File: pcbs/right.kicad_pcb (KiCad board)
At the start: 2 copper layers, 132.7 x 86.8 mm, 46 parts

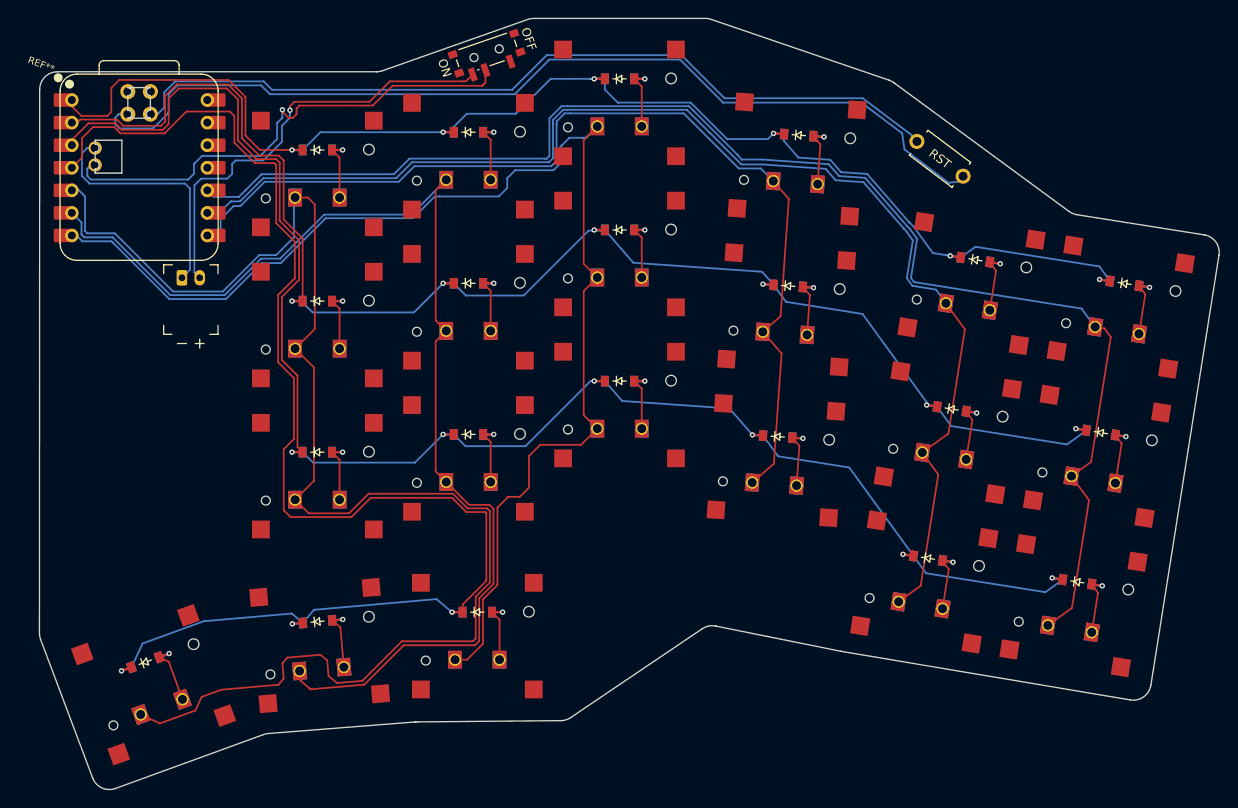
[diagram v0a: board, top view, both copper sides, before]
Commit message: improved some of the routing. added cutout for batter to save 1mm during assembly
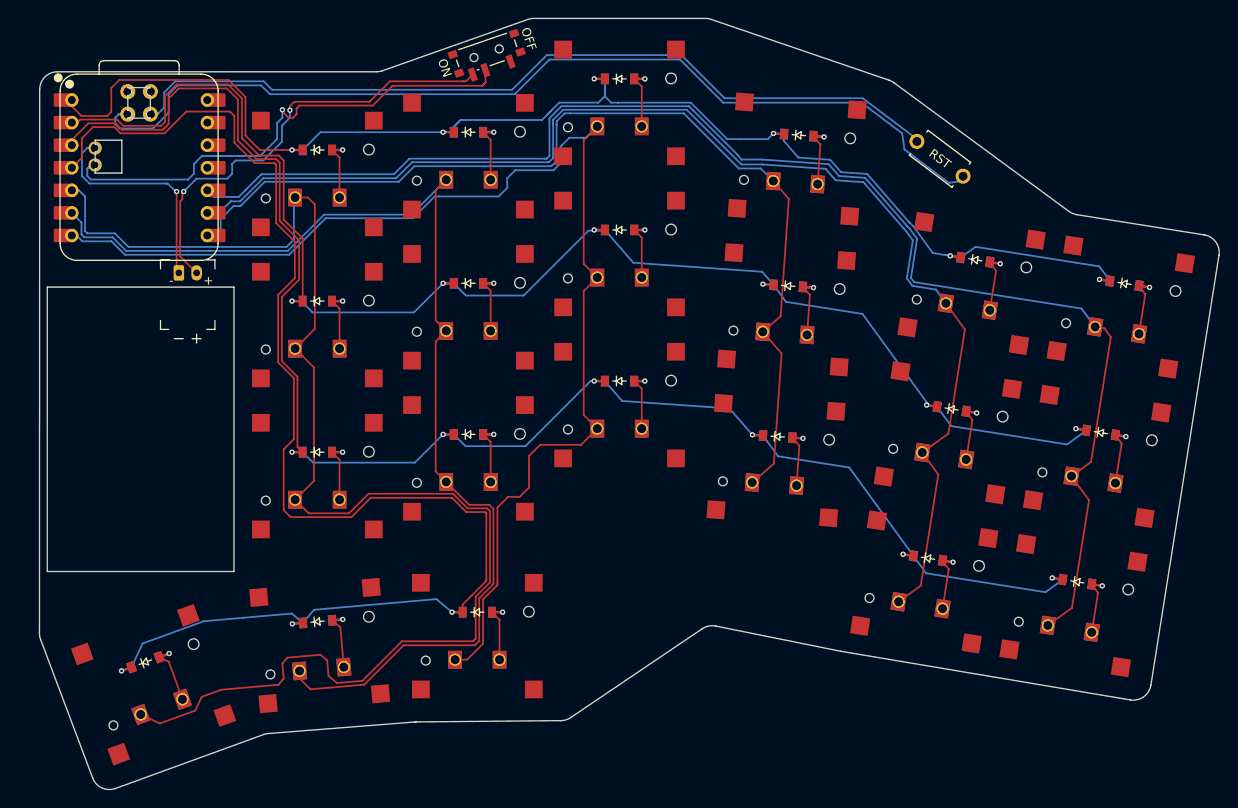
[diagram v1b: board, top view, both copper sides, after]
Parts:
- moved JST1 0.65 mm to (132.7, 189.1)
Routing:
- net P5: track 135.3 -> 131.0 mm
- net P6: track 147.5 -> 143.4 mm
- net P4: track 162.7 -> 158.6 mm
- net P0: track 155.4 -> 158.3 mm
- net GND: track 124.0 -> 121.8 mm, vias 0 -> 1
- net BAT_P: track 49.6 -> 50.9 mm, vias 1 -> 2
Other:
- outline, holes or cut-outs redrawn
- board text added: "+"
- board text added: "-"
